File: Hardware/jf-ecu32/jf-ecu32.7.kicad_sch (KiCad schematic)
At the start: 89 parts, among them J1 GAZ, J10 k, J11 RPM, J12 S.PORT, J13 PPM/PWM, J14 PUMP1, J15 PUMP1, J16 PPM/PWM, J17 PUMP2, J18 PUMP2, J19 EN, J2 AUX, J20 Conn_01x06, J21 Conn_01x07, J3 PPM/PWM, J4 STARTER, J5 GLOW, J6 VANNE KEROSTART, J7 VANNE KERO, J8 BATTERY 2S/3S, J9 STARTER, Q1 AO3400A, Q2 QM6006D, Q3 AO3400A, Q4 QM6006D, Q5 QM6006D, Q6 QM6006D, Q7 AO3400A, Q8 AO3400A, U1 ESP32-WROOM-32D, U2 4050, U3 MAX31855KASA, U4 AMS1117-3.3, U5 4050, U6 AMS1117-5.0, U7 OPA340NA, U8 LM4040DBZ-2.5, U9 INA219AxDCN

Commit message: Test Carte V3 - Maj vers V4
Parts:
- removed Q2: QM6006D, Package_TO_SOT_SMD:TO-252-2, symbol Transistor_FET:QM6006D
- added C14: 0.1µF, Capacitor_SMD:C_0603_1608Metric, symbol Device:C
- added Q2: A49T, Package_TO_SOT_SMD:SOT-23, symbol Transistor_FET:AO3400A
- added Q9: FDD6685, Package_TO_SOT_SMD:TO-252-2, symbol Transistor_FET:QM6015D
- added R25: 10K, Resistor_SMD:R_0603_1608Metric, symbol Device:R
- added R26, R27: 10R, Resistor_SMD:R_2512_6332Metric, symbol Device:R
- D10, D13, D15, D3: value D_Schottky -> D_Schottky SS34
- D7, D9: value D_Schottky -> D_Schottky SS14
- Q1, Q3, Q7, Q8: value AO3400A -> A49T
- Q4, Q5, Q6: value QM6006D -> LR8726
- R10, R11, R12, R7, R8, R9: value R -> 10K
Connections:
- net +BATT: now also R11.2, Q9.3 (S)
- net GND: now also Q2.2 (S), R25.2, R27.1; no longer R11.2, U9.2 (IN-)
- net PWM_GLOW: now also Q2.1 (G), R25.1; no longer R11.1
- net at D10.2 (A), J5.1 (Pin_1), R1.1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: now also R26.1; no longer U9.1 (IN+)
- net at D10.1 (K), J5.2 (Pin_2): now also Q9.2 (D)
- new net: C14.1, R26.2, U9.1 (IN+)
- new net: C14.2, R27.2, U9.2 (IN-)
- new net: Q2.3 (D), Q9.1 (G), R11.1
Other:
- moved on the sheet: D10, D9, J5, R1, R11, R2

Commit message: PCB V4 updated
PCB V4
File server
Glow current read
Voltage Read
Starter calibration working
Many links corrected
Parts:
- removed C14: 0.1µF, Capacitor_SMD:C_0603_1608Metric, symbol Device:C
- removed R26, R27: 10R, Resistor_SMD:R_2512_6332Metric, symbol Device:R
- added D11, D12, D2, D4, D5, D6, D8: LED, LED_SMD:LED_0603_1608Metric, symbol Device:LED
- added R32, R33: 10K, Resistor_SMD:R_0603_1608Metric, symbol Device:R
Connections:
- net +3.3V: now also D8.2 (A)
- net +5V: now also D11.2 (A)
- net GND: now also R12.1, U9.2 (IN-), R32.2, R33.2; no longer R12.2
- net P1_MOSFET: now also D2.2 (A); no longer R7.1
- net P2_MOSFET: now also D4.2 (A); no longer R8.1
- net PWM_GLOW: now also D6.2 (A); no longer R25.1
- net PWM_KERO: now also D5.2 (A); no longer R12.1
- net PWM_KEROSTART: now also D12.2 (A); no longer R10.1
- net at U9.1 (IN+): now also D10.2 (A), J5.1 (Pin_1), R1.1, R2.1
- new net: D11.1 (K), R33.1
- new net: D8.1 (K), R32.1
- new net: D2.1 (K), R7.1
- new net: D6.1 (K), R25.1
- new net: D4.1 (K), R8.1
- new net: D5.1 (K), R12.2
- new net: D12.1 (K), R10.1
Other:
- moved on the sheet: C13, D13, D15, D3, J13, J14, J15, J16, J17, J18, J3, J4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

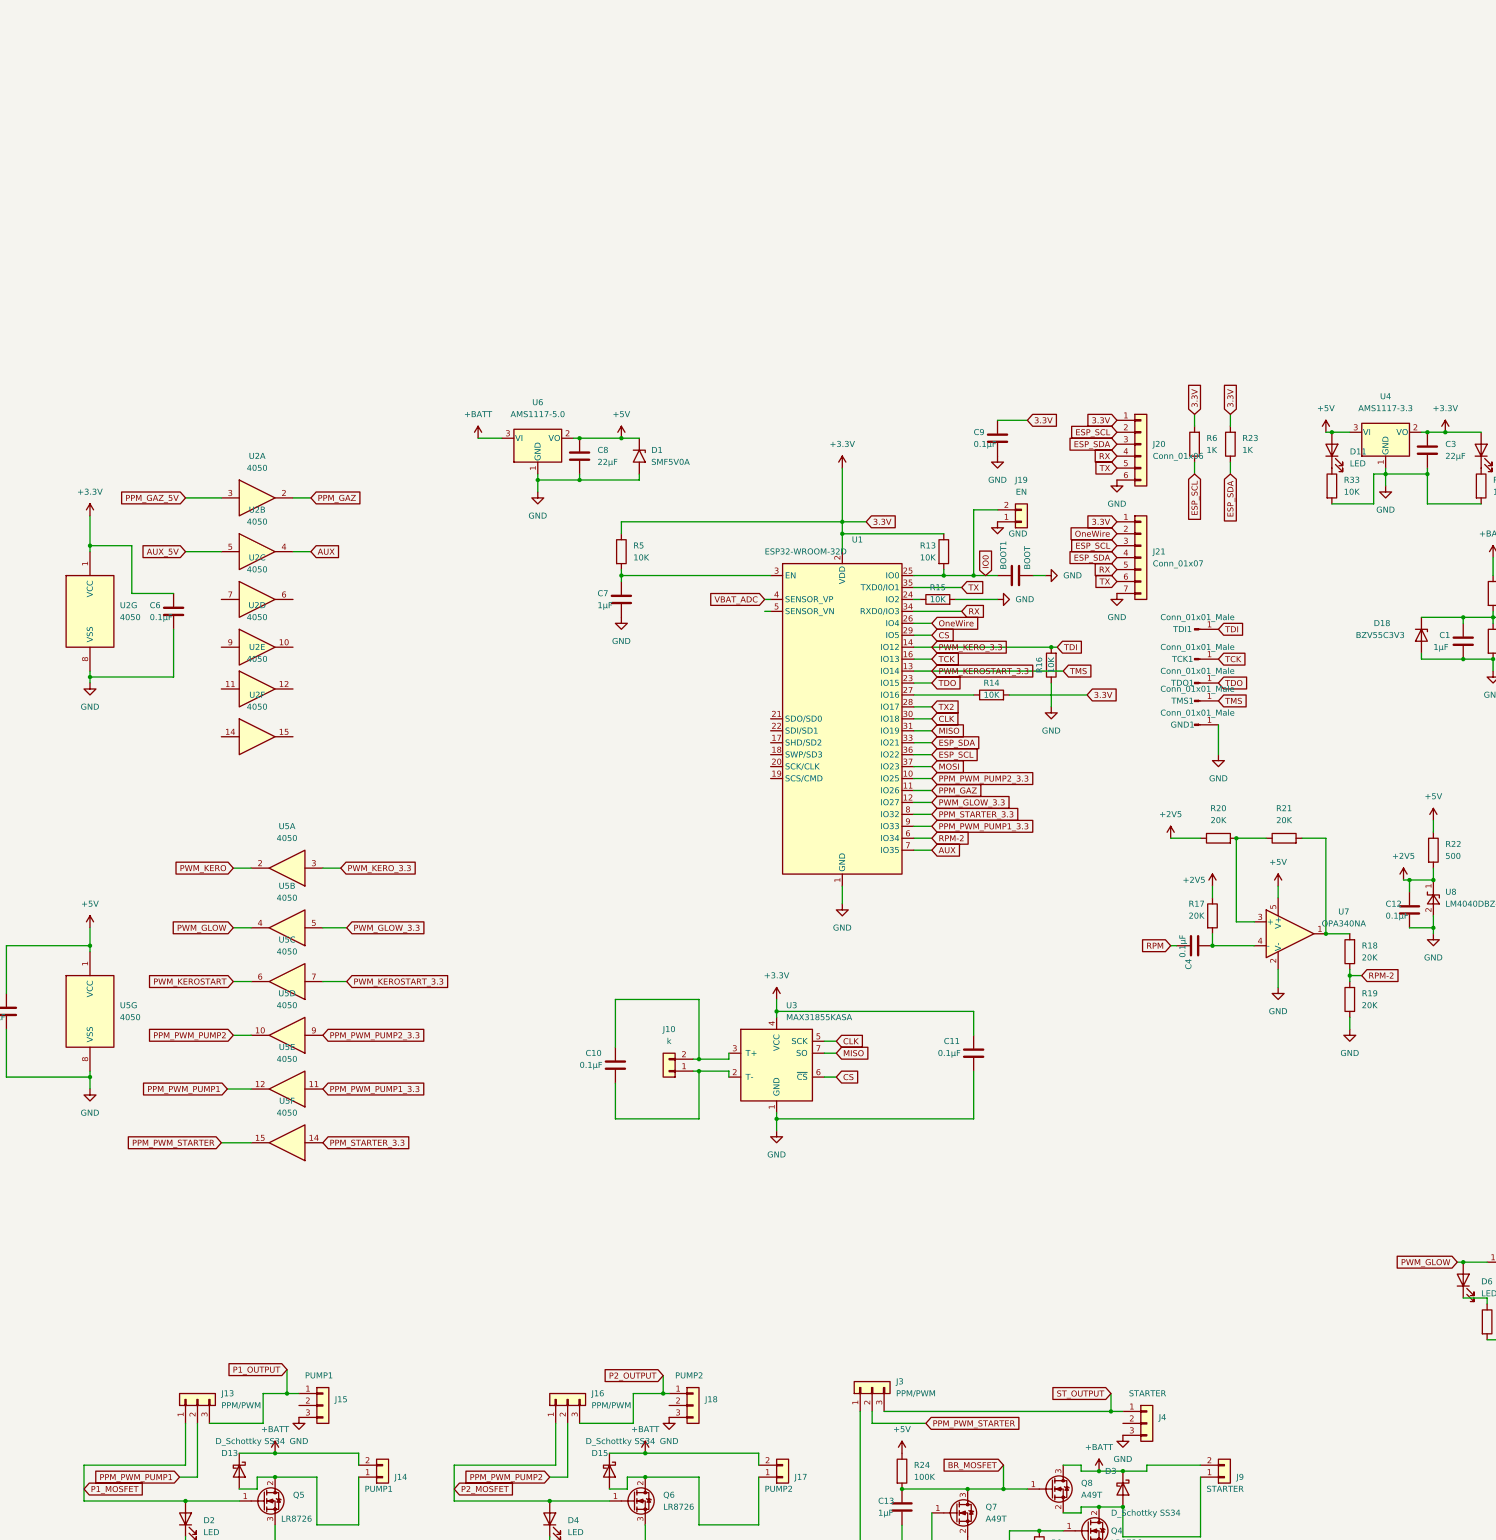
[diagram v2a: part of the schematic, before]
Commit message: Added MicroSD and BMP280
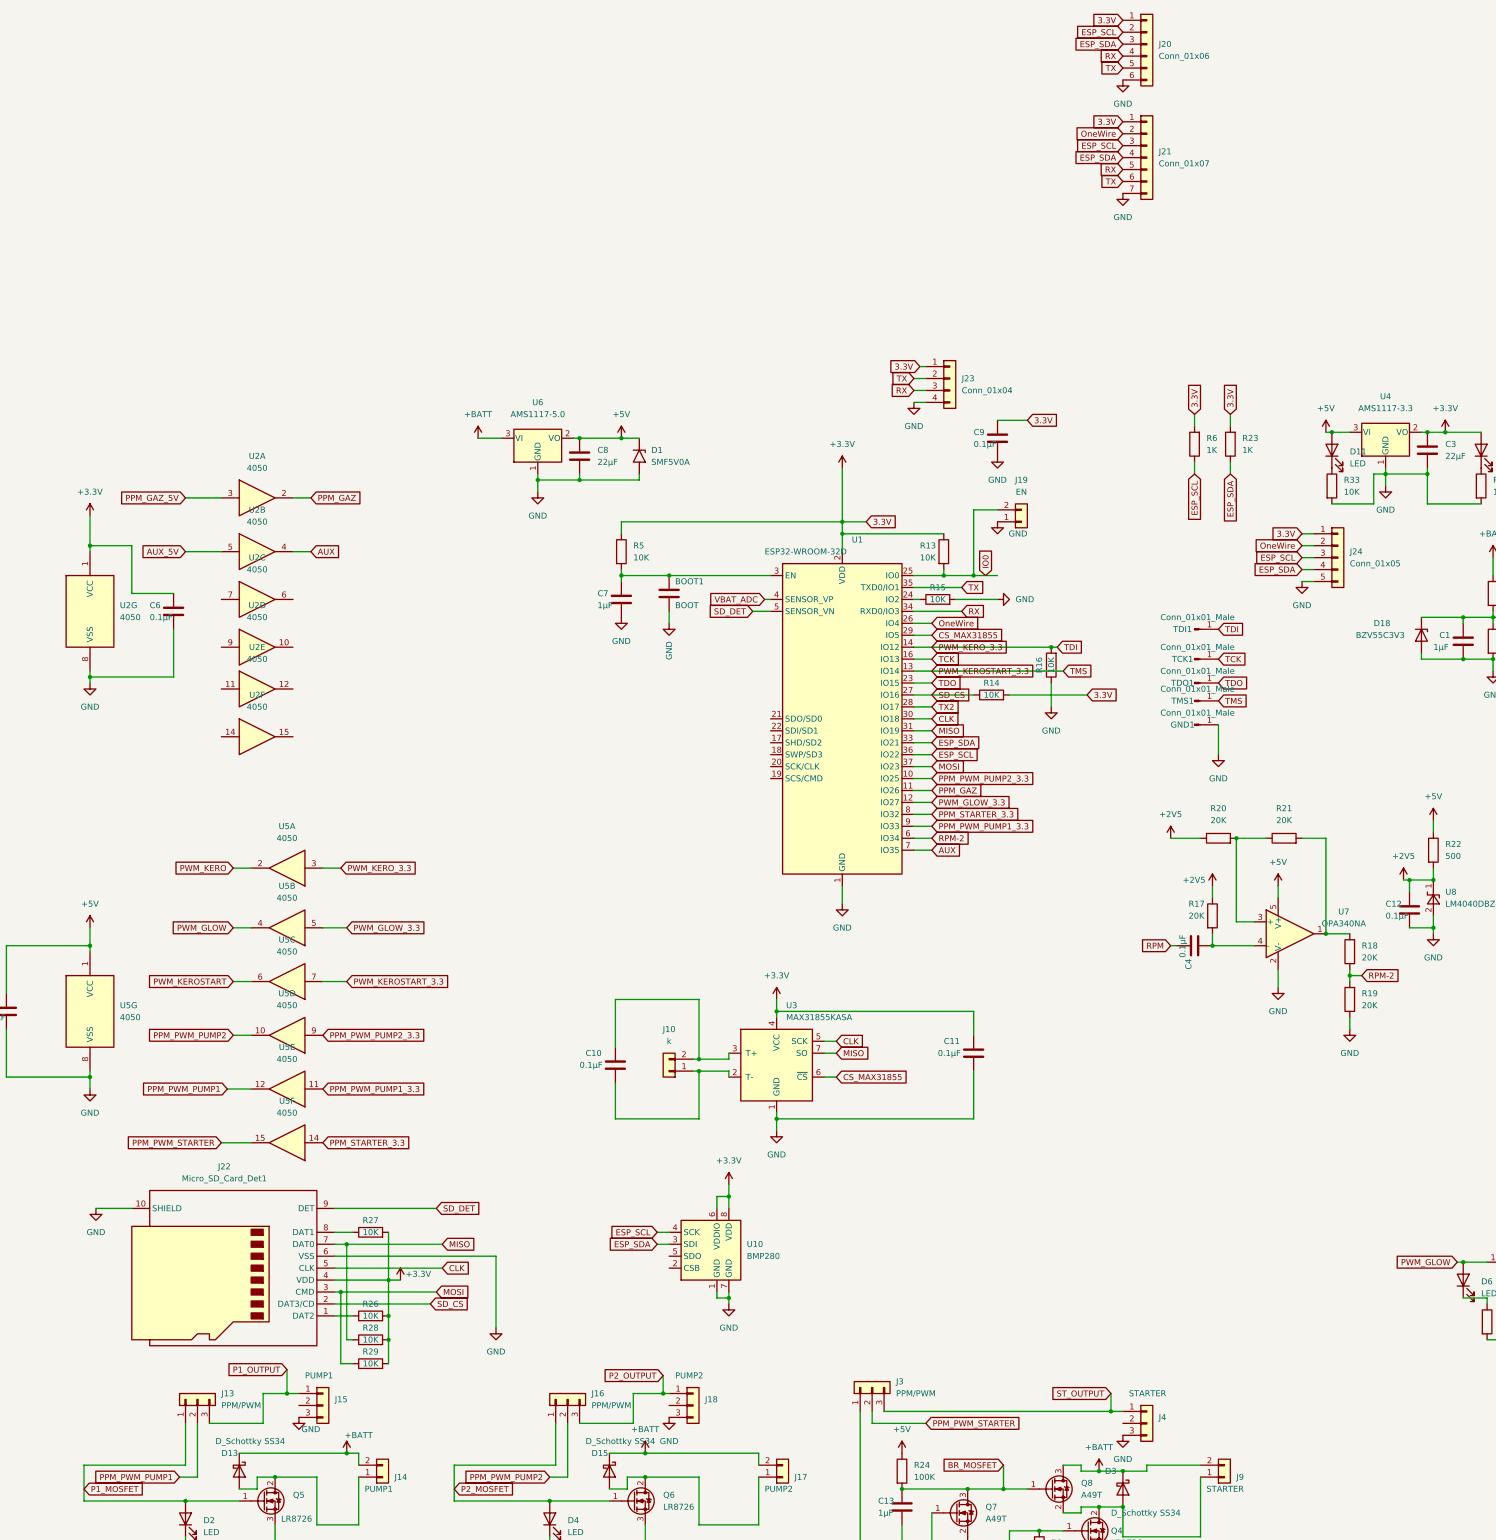
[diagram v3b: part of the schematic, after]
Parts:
- added J22: Micro_SD_Card_Det1, Connector_Card:J_SD_Card-micro_socket_A, symbol Connector:Micro_SD_Card_Det1
- added J23: Conn_01x04, Connector_PinSocket_2.00mm:PinSocket_1x04_P2.00mm_Vertical, symbol Connector_Generic:Conn_01x04
- added J24: Conn_01x05, Connector_PinSocket_2.00mm:PinSocket_1x05_P2.00mm_Vertical, symbol Connector_Generic:Conn_01x05
- added R26, R27, R28, R29: 10K, Resistor_SMD:R_0603_1608Metric, symbol Device:R
- added U10: BMP280, Package_LGA:Bosch_LGA-8_2x2.5mm_P0.65mm_ClockwisePinNumbering, symbol Sensor_Pressure:BMP280
- J21: footprint Connector_JST:JST_PH_B7B-PH-K_1x07_P2.00mm_Vertical -> (none)
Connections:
- net +3.3V: now also J22.4 (VDD), J23.1 (Pin_1), J24.1 (Pin_1), R26.2, R27.2, R28.2, R29.2, U10.6 (VDDIO), U10.8 (VDD)
- net CLK: now also J22.5 (CLK)
- net ESP_SCL: now also J24.3 (Pin_3), U10.4 (SCK)
- net ESP_SDA: now also J24.4 (Pin_4), U10.3 (SDI)
- net GND: now also J22.10 (SHIELD), J22.6 (VSS), J23.4 (Pin_4), J24.5 (Pin_5), U10.1 (GND), U10.7 (GND)
- net IO0: no longer BOOT1.1
- net MISO: now also J22.7 (DAT0), R28.1
- net MOSI: now also J22.3 (CMD), R29.1
- net OneWire: now also J24.2 (Pin_2)
- net RX: now also J23.3 (Pin_3)
- net TX: now also J23.2 (Pin_2)
- net at C7.1, R5.2, U1.3 (EN): now also BOOT1.1
- net SD_CS: now reaches R14.1, U1.27 (IO16)
- net SD_CS: now also J22.2 (DAT3/CD)
- net SD_DET: now reaches U1.5 (SENSOR_VN)
- net SD_DET: now also J22.9 (DET)
- net CS renamed CS_MAX31855
- new net: J22.1 (DAT2), R26.1
- new net: J22.8 (DAT1), R27.1
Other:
- moved on the sheet: J20, J21

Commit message: PCB Update
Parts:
- added C14: 0.1µF, Capacitor_SMD:C_0603_1608Metric, symbol Device:C
- J23: footprint Connector_PinSocket_2.00mm:PinSocket_1x04_P2.00mm_Vertical -> Connector_JST:JST_PH_B4B-PH-K_1x04_P2.00mm_Vertical
- J24: footprint Connector_PinSocket_2.00mm:PinSocket_1x05_P2.00mm_Vertical -> Connector_JST:JST_PH_B5B-PH-K_1x05_P2.00mm_Vertical
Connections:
- net +3.3V: now also C14.1
- net GND: now also C14.2
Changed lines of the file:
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@@
     (stroke (width 0) (type default))
   )
+  (wire (pts (xy 154.94 191.77) (xy 170.18 191.77))
+    (stroke (width 0) (type default))
+  )
   (wire (pts (xy 19.05 53.34) (xy 19.05 54.61))
     (stroke (width 0) (type default))
@@
     (stroke (width 0) (type default))
   )
+  (wire (pts (xy 170.18 198.12) (xy 170.18 191.77))
+    (stroke (width 0) (type default))
+  )
   (wire (pts (xy 347.98 182.88) (xy 347.98 190.5))
     (stroke (width 0) (type default))
@@
     (stroke (width 0) (type default))
   )
+  (wire (pts (xy 154.94 213.36) (xy 170.18 213.36))
+    (stroke (width 0) (type default))
+  )
   (wire (pts (xy 384.81 119.38) (xy 384.81 120.65))
     (stroke (width 0) (type default))
@@
     (stroke (width 0) (type default))
   )
+  (wire (pts (xy 170.18 205.74) (xy 170.18 213.36))
+    (stroke (width 0) (type default))
+  )
   (wire (pts (xy 17.78 256.54) (xy 39.37 256.54))
     (stroke (width 0) (type default))
@@
       (effects (font (size 1.27 1.27)) (justify left))
     )
-    (property "Footprint" "Connector_PinSocket_2.00mm:PinSocket_1x05_P2.00mm_Vertical" (at 284.48 55.88 0)
-      (effects (font (size 1.27 1.27)) hide)
+    (property "Footprint" "Connector_JST:JST_PH_B5B-PH-K_1x05_P2.00mm_Vertical" (at 284.48 55.88 0)
+      (effects (font (size 1.27 1.27)))
     )
     (property "Datasheet" "~" (at 284.48 55.88 0)
@@
       (effects (font (size 1.27 1.27)) (justify left))
     )
-    (property "Footprint" "Connector_PinSocket_2.00mm:PinSocket_1x04_P2.00mm_Vertical" (at 201.93 17.78 0)
+    (property "Footprint" "Connector_JST:JST_PH_B4B-PH-K_1x04_P2.00mm_Vertical" (at 201.93 17.78 0)
       (effects (font (size 1.27 1.27)) hide)
     )
@@
         )
       )
+    )
+  )
+  (symbol (lib_id "Device:C") (at 170.18 201.93 0) (unit 1)
+    (in_bom yes) (on_board yes) (dnp no)
+    (property "Reference" "C14" (at 175.26 198.12 0)
+      (effects (font (size 1.27 1.27)) (justify left))
+    )
+    (property "Value" "0.1µF" (at 175.26 201.93 0)
+      (effects (font (size 1.27 1.27)) (justify left))
+    )
+    (property "Footprint" "Capacitor_SMD:C_0603_1608Metric" (at 171.1452 205.74 0)
+      (effects (font (size 1.27 1.27)) hide)
+    )
+    (property "Datasheet" "~" (at 170.18 201.93 0)
+      (effects (font (size 1.27 1.27)) hide)
+    )
+    (pin "1")
+    (pin "2")
+    (instances
+      (project "jf-ecu32.7"
+        (path "/89131591-836b-4344-93b0-14d6b2e32546"
+          (reference "C14") (unit 1)
+        )
+      )
